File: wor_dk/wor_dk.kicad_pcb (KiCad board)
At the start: 4 copper layers, 217 x 110.1 mm, 135 parts, among them J101 Conn_01x02, J102 Conn_02x03_Odd_Even, J103 Conn_02x03_Odd_Even, J104 Conn_01x02, J201 SWD, J301 SMA, J302 Conn_02x04_Odd_Even, J303 Conn_02x06_Odd_Even, J401 USB_C_Receptacle_USB2.0_16P, J501 SWD, J502 USB_C_Receptacle_USB2.0_16P, J503 SWD, Q501 BSS84, SW201 SW_Push, SW501 SW_Push, U201 nRF52840, U202 TMUX1112PWR, U203 TMUX1112PWR, U301 Si4467, U401 FT232RL, U501 TLV1117-33, U502 LPC11U35FHI33_501, Y201 32.768kHz, Y202 32MHz, Y301 26MHz, Y501 12MHz

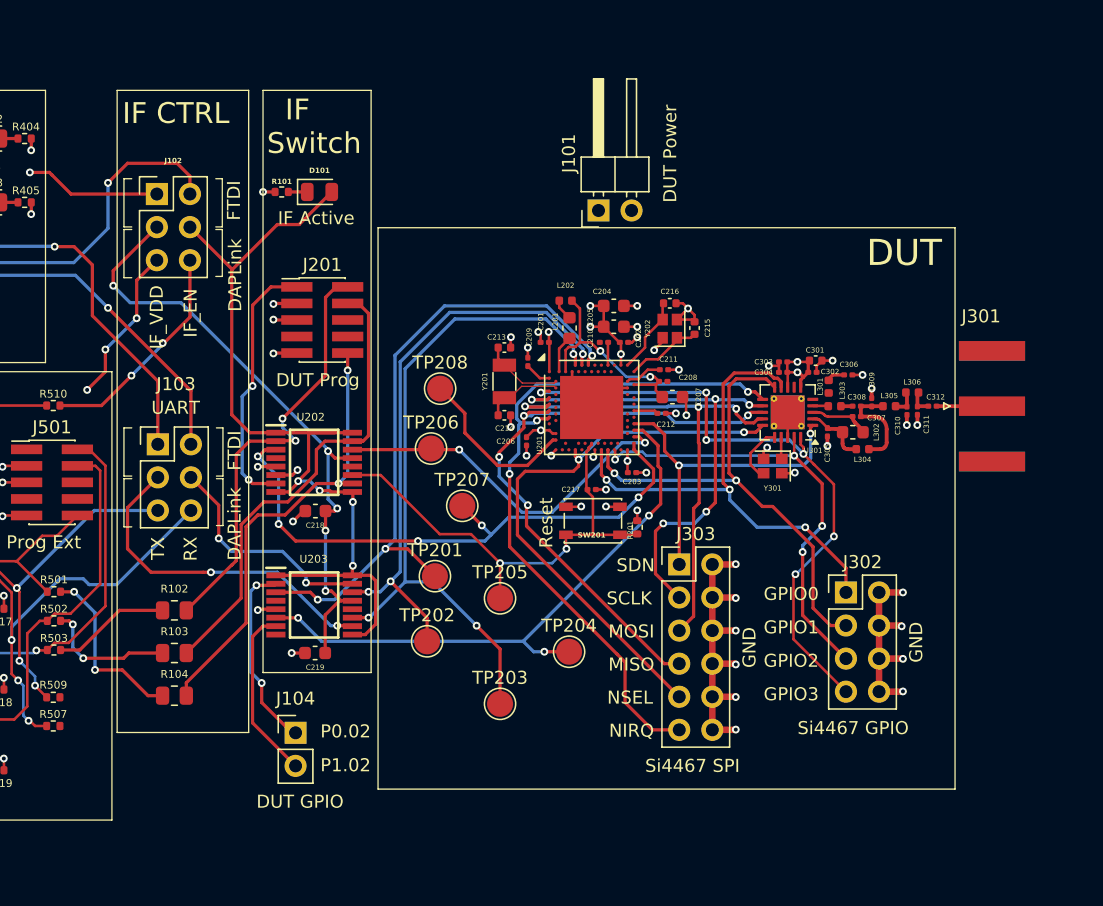
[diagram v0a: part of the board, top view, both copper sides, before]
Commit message: wor_dk: PCB: add remaining zone fills & (mostly) finalize routing
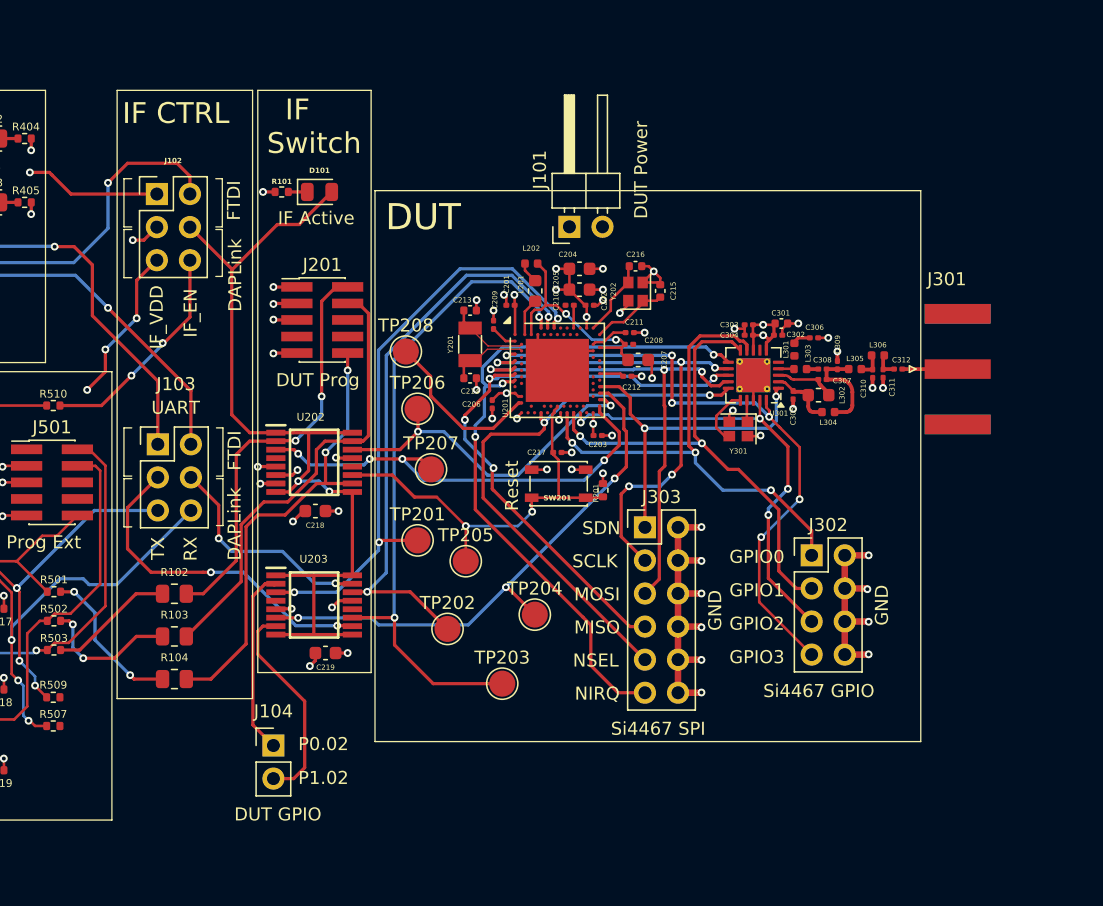
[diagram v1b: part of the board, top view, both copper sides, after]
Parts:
- moved C202 3.88 mm to (133.0, 71.6)
- moved C204 3.88 mm to (132.2, 68.8)
- moved C205 3.88 mm to (132.2, 70.4)
- moved C207 3.88 mm to (136.7, 75.8)
- moved C301 3.88 mm to (147.7, 73.0)
- moved C302 3.88 mm to (147.4, 73.9)
- moved C303 3.88 mm to (145.2, 73.1)
- moved C304 3.88 mm to (145.2, 73.9)
- moved C306 3.88 mm to (150.2, 74.1)
- moved C311 3.88 mm to (155.5, 76.8)
- moved L301 3.88 mm to (148.7, 75.0)
- moved C213 3.88 mm to (123.8, 72.0)
- moved C214 3.88 mm to (123.8, 77.2)
- moved Y201 3.88 mm to (123.8, 74.6)
- moved C201 3.88 mm to (126.9, 71.6)
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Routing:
- net /VDD_AUX: track 48.6 -> 7.24 mm
- net /Main MCU/SWDIO_: track 45.6 -> 35.0 mm, vias 5 -> 4
- net /Main MCU/NRESET_: track 36.4 -> 32.6 mm
- net /Main MCU/P1.02_: track 45.4 -> 42.2 mm
- net /P1.02: track 13.4 -> 16.3 mm
- net /Main MCU/P0.02_: track 49.8 -> 47.5 mm
- net /NRESET: track 13.8 -> 11.8 mm
- net VDD_DUT: track 46.6 -> 45.1 mm
- net /Main MCU/P0.31_: track 52.1 -> 50.6 mm, vias 3 -> 2
- net /Main MCU/SWDIO: track 33.4 -> 32.0 mm
- net /Main MCU/SWCLK: track 36.6 -> 35.3 mm
- net /IF_EN: track 68.1 -> 69.2 mm, vias 4 -> 2
- net /Main MCU/VDD_DUT_OUT: track 20.1 -> 19.1 mm
- net /Main MCU/SWCLK_: track 27.7 -> 26.8 mm
- net /Main MCU/NRESET: track 35.8 -> 35.0 mm
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- added copper zone on In2.Cu, net /VDD_AUX
- added copper zone on In2.Cu, net VDD_DUT

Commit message: wor_dk: PCB: fix some DRC issues
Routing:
- net GND: track 148.3 -> 216.7 mm, vias 79 -> 111
- net /Transceiver/NIRQ: track 54.5 -> 52.0 mm
- net VDD_PROG: track 31.8 -> 30.7 mm
- net /Transceiver/MOSI: track 39.0 -> 39.6 mm
- net /Transceiver/GPIO0: track 39.8 -> 39.3 mm
- net /Main MCU/P0.02_: track 47.5 -> 47.0 mm
- net VDD_DUT: track 45.1 -> 44.9 mm, vias 11 -> 12

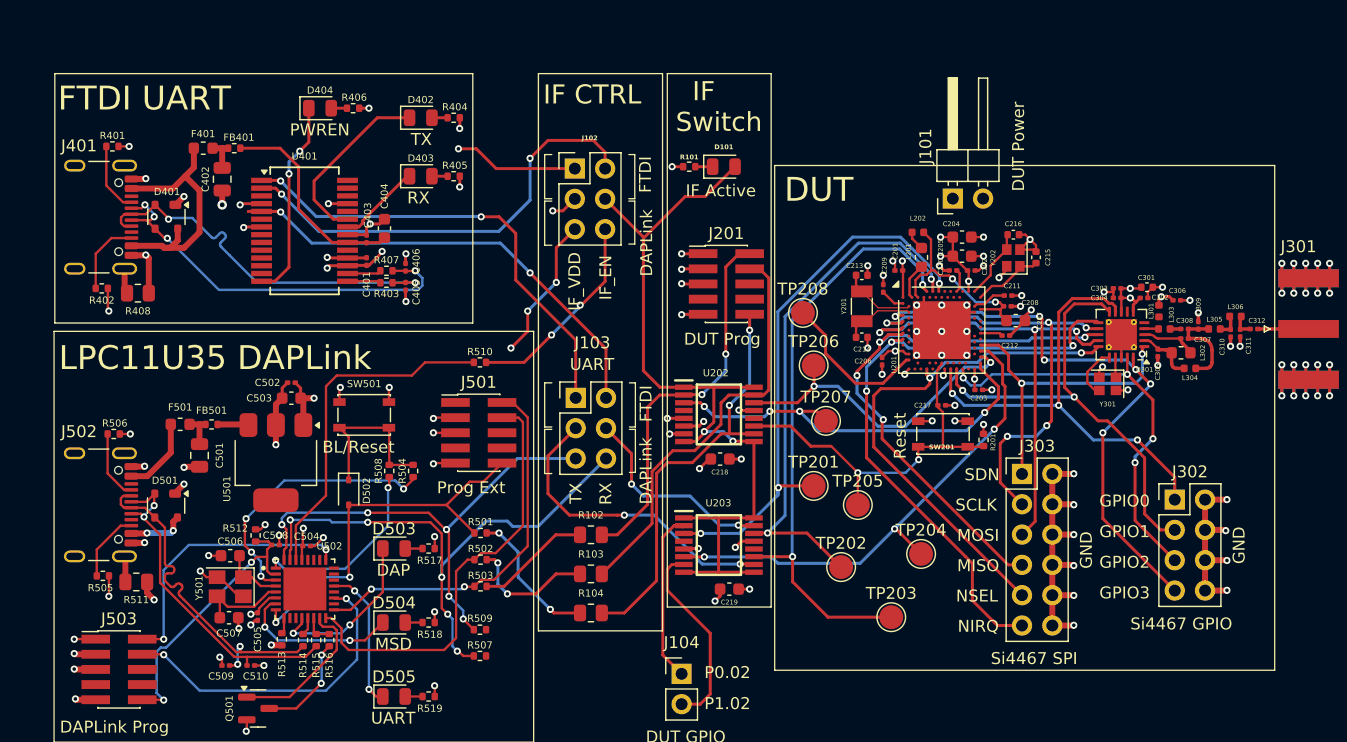
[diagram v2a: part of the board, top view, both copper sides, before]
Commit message: wor_dk: PCB: fix most DRC errors
The remaining errors are all related to the LPC11U35 footprint.
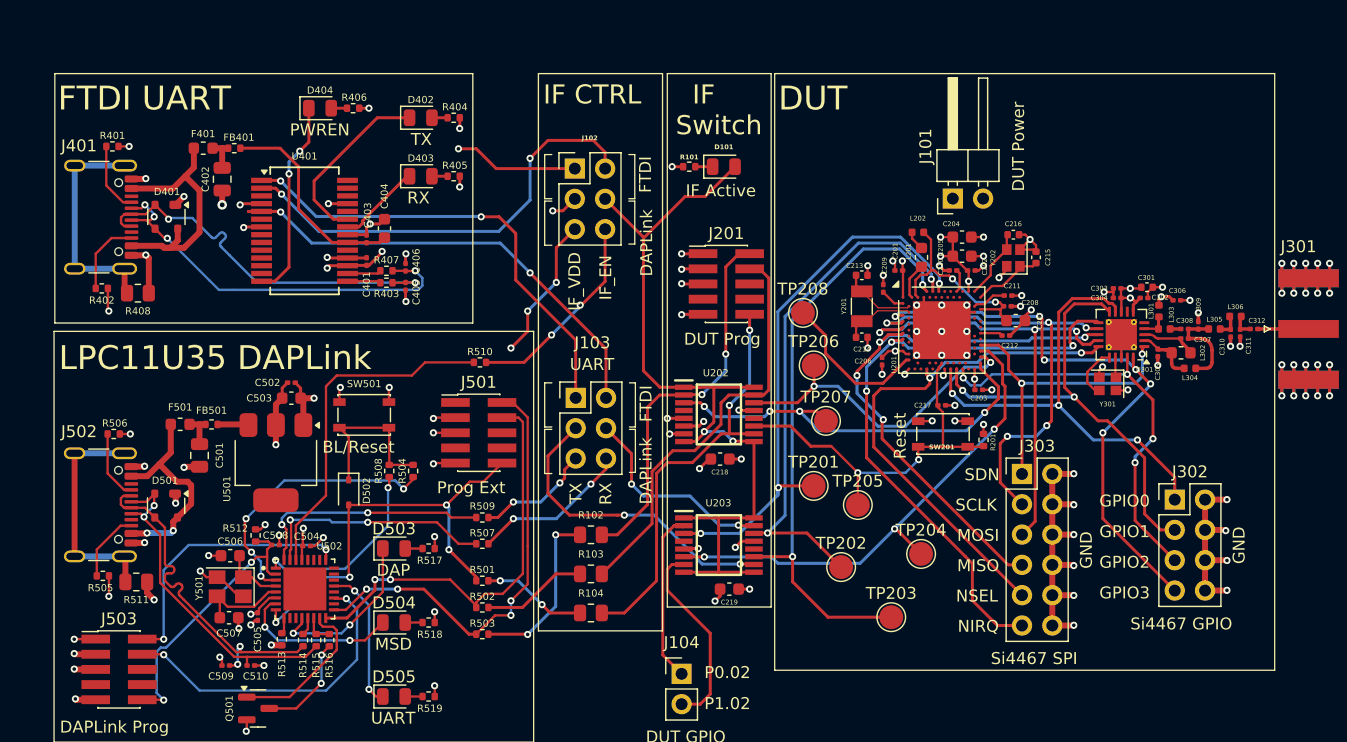
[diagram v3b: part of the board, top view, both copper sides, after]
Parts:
- moved R507 9.40 mm to (92.0, 94.5)
- moved R509 9.40 mm to (92.0, 92.3)
- moved R502 4.01 mm to (92.0, 99.8)
- moved R503 4.01 mm to (92.0, 102.1)
- moved R501 4.01 mm to (92.0, 97.6)
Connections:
- R507 pad 1: /RXD_DAP -> /LPC11U35 DAPLink Programmer/RXD
- R509 pad 1: /TXD_DAP -> /LPC11U35 DAPLink Programmer/TXD
- R510 pad 1: /DTR_DAP -> /LPC11U35 DAPLink Programmer/DTR
- U502 pad 30: /DTR_DAP -> /LPC11U35 DAPLink Programmer/DTR
- U502 pad 31: /RXD_DAP -> /LPC11U35 DAPLink Programmer/RXD
- U502 pad 32: /TXD_DAP -> /LPC11U35 DAPLink Programmer/TXD
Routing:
- net /RXD_DAP: track 47.4 -> 13.3 mm, vias 5 -> 2
- net /TXD_DAP: track 40.9 -> 9.79 mm, vias 5 -> 2
- net /DTR_DAP: track 46.0 -> 17.2 mm
- net /LPC11U35 DAPLink Programmer/DTR: track 0.00 -> 28.8 mm
- net /LPC11U35 DAPLink Programmer/TXD: track 0.00 -> 20.4 mm, vias 0 -> 2
- net /LPC11U35 DAPLink Programmer/RXD: track 0.00 -> 19.8 mm, vias 0 -> 2
- net Net-(J502-SHIELD): track 2.18 -> 19.2 mm
- net Net-(J401-SHIELD): track 2.13 -> 19.1 mm
- net Net-(D501-VCC): track 11.4 -> 17.9 mm
- net /LPC11U35 DAPLink Programmer/TGT_SWDIO: track 31.9 -> 37.6 mm, vias 2 -> 4
- net /SWDIO: track 9.62 -> 14.7 mm, vias 0 -> 2
- net /LPC11U35 DAPLink Programmer/TGT_NRESET: track 32.5 -> 36.6 mm, vias 2 -> 4
- net /NRESET: track 11.8 -> 8.80 mm
- net /SWCLK: track 10.8 -> 8.84 mm, vias 2 -> 0
- net /LPC11U35 DAPLink Programmer/TGT_SWCLK: track 36.5 -> 35.5 mm, vias 0 -> 2
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
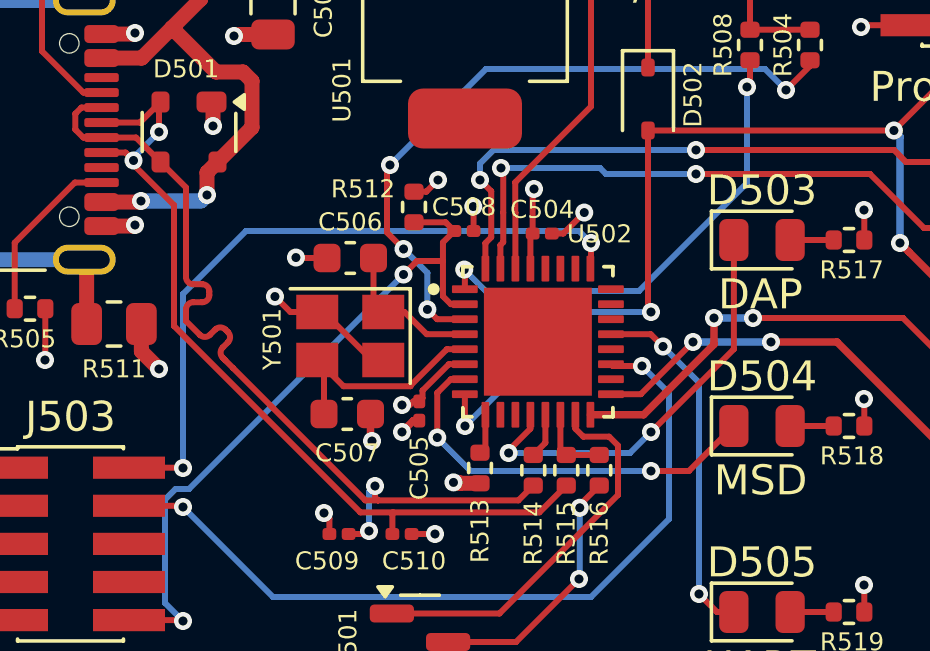
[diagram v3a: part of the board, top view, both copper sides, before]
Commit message: wor_dk: PCB: use KiCAD HVQFN-32 footprint instead of downloaded
This fixes all remaining DRC issues.
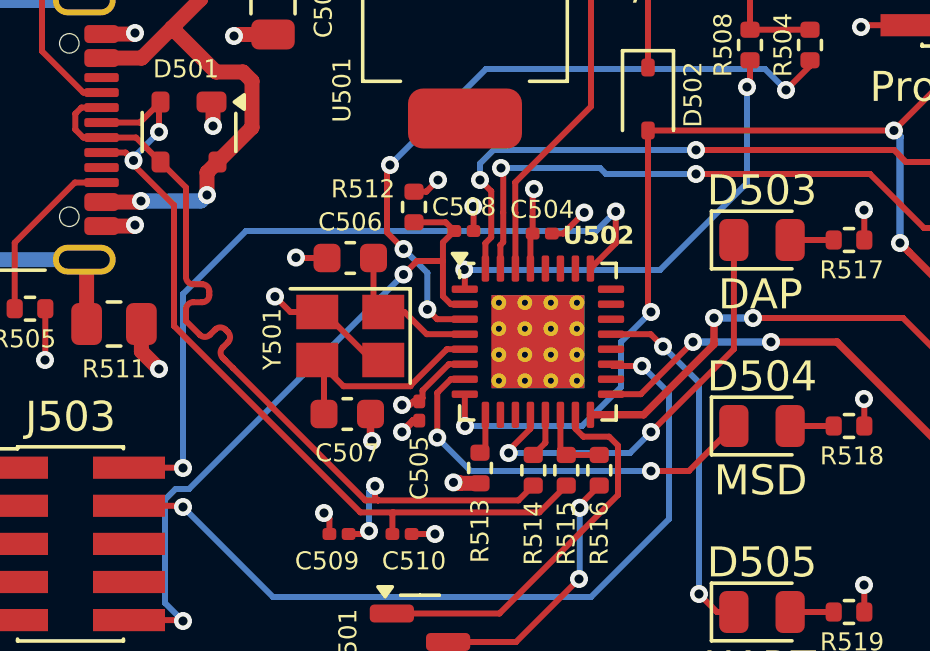
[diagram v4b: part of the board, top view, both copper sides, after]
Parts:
- U502: footprint NXP:QFN50P500X500X85-33N -> Package_DFN_QFN:HVQFN-32-1EP_5x5mm_P0.5mm_EP3.1x3.1mm_ThermalVias
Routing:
- net /LPC11U35 DAPLink Programmer/IF_SWDIO: track 23.1 -> 25.4 mm
- net /LPC11U35 DAPLink Programmer/TGT_NRESET: track 36.6 -> 37.5 mm
- net /LPC11U35 DAPLink Programmer/TGT_NRESET_FB_ISP: track 16.0 -> 15.4 mm

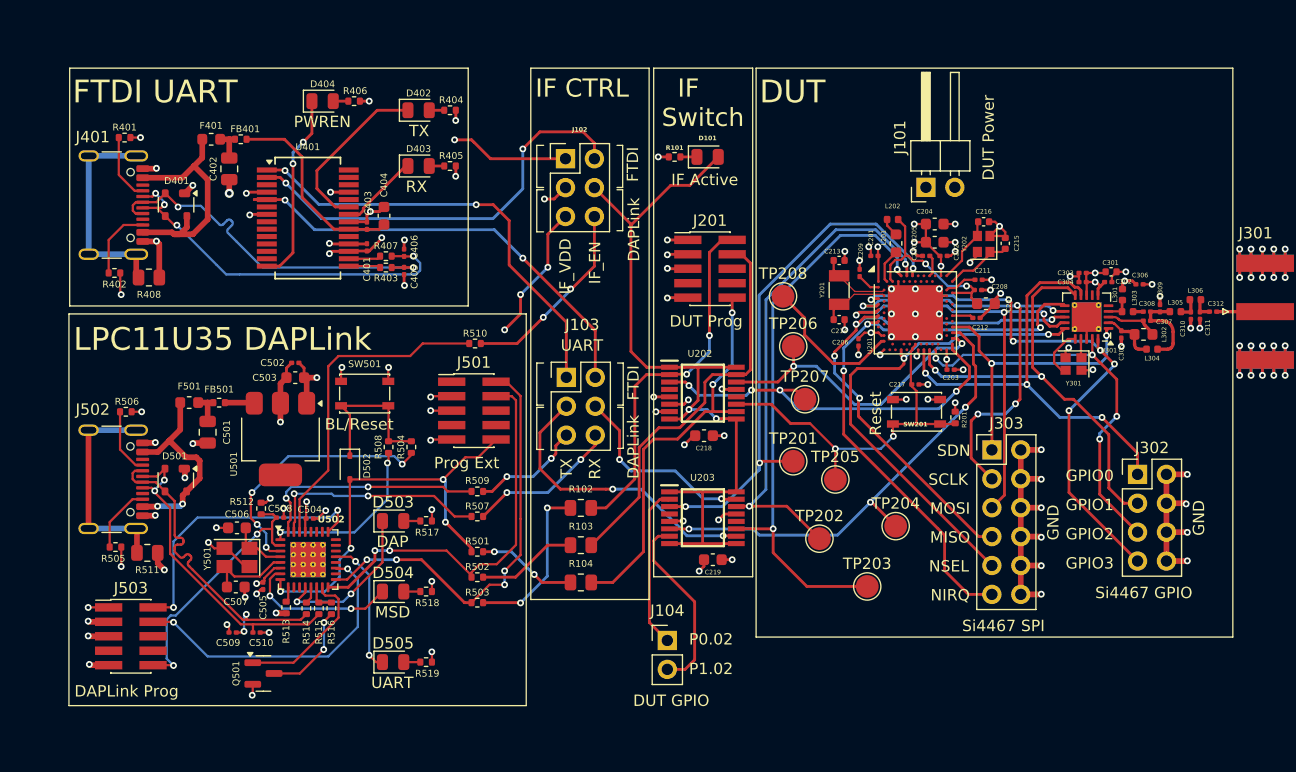
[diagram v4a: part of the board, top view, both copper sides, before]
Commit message: wor_dk: add M2.5 screw holes
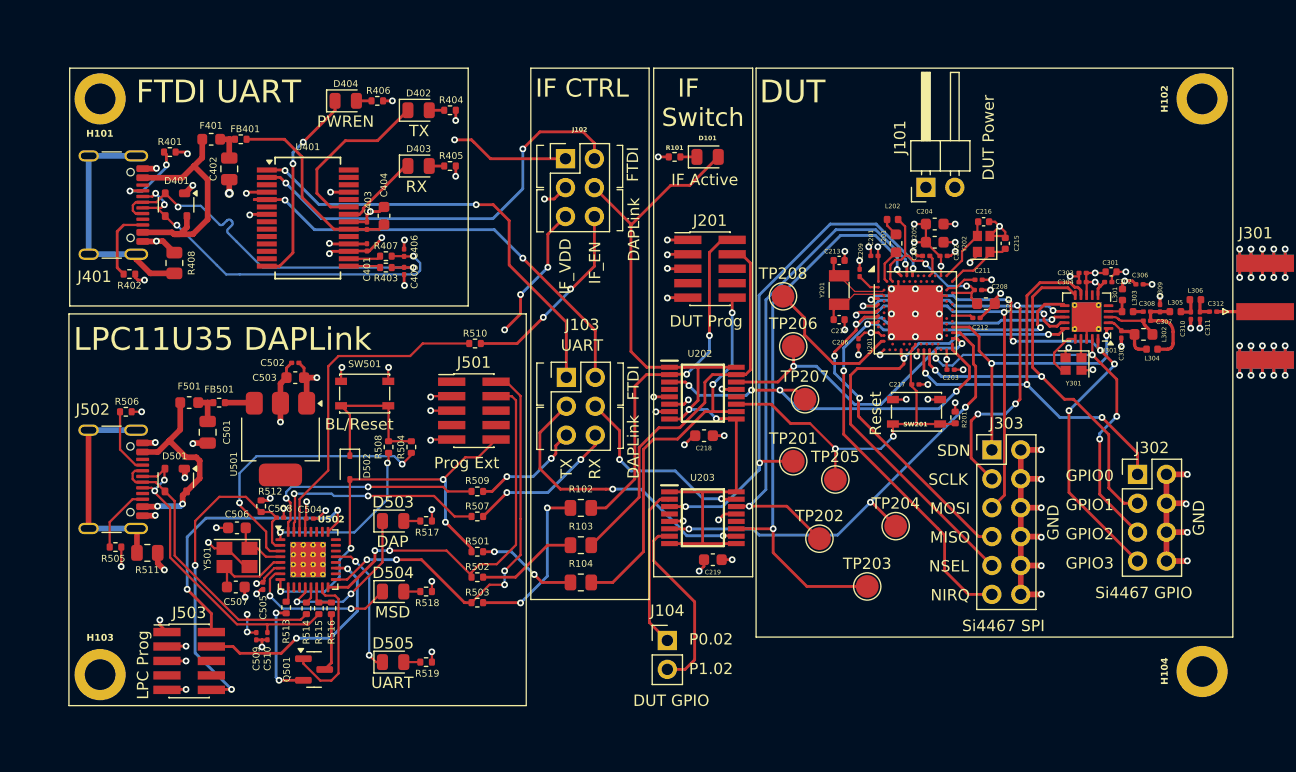
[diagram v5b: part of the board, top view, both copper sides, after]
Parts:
- added H101: MountingHole_Pad, MountingHole:MountingHole_2.7mm_M2.5_ISO7380_Pad, F.Cu at (58.9, 57.8)
- added H102: MountingHole_Pad, MountingHole:MountingHole_2.7mm_M2.5_ISO7380_Pad, F.Cu at (155.7, 57.8)
- added H103: MountingHole_Pad, MountingHole:MountingHole_2.7mm_M2.5_ISO7380_Pad, F.Cu at (58.9, 108.4)
- added H104: MountingHole_Pad, MountingHole:MountingHole_2.7mm_M2.5_ISO7380_Pad, F.Cu at (155.7, 108.1)
- moved J503 5.57 mm to (66.7, 107.2)
- moved Q501 4.46 mm to (77.7, 108.0)
- moved R401 4.17 mm to (65.0, 62.5)
- moved R408 2.58 mm to (65.4, 72.2), turned to 90 degrees
- moved C509 2.10 mm to (72.6, 105.0), turned to 90 degrees
- moved D404 2.04 mm to (80.4, 58.0)
- moved R406 2.04 mm to (83.2, 58.0)
- moved R402 1.32 mm to (61.4, 73.2)
- moved C510 1.00 mm to (73.5, 105.0), turned to 90 degrees
- moved R512 0.20 mm to (73.0, 93.6)
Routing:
- net /LPC11U35 DAPLink Programmer/IF_SWCLK: track 26.9 -> 19.7 mm
- net VDD_PROG: track 30.7 -> 37.4 mm
- net /LPC11U35 DAPLink Programmer/IF_NRESET: track 23.3 -> 29.9 mm
- net Net-(Q501-D): track 8.63 -> 5.11 mm, vias 2 -> 0
- net /LPC11U35 DAPLink Programmer/TGT_NRESET_FB: track 22.9 -> 25.4 mm, vias 4 -> 2
- net Net-(J401-SHIELD): track 19.1 -> 21.3 mm
- net GND: track 216.4 -> 214.3 mm, vias 111 -> 110
- net /LPC11U35 DAPLink Programmer/USB_D-: track 29.6 -> 27.8 mm
- net Net-(D404-K): track 16.8 -> 17.7 mm
- net Net-(J401-CC1): track 5.97 -> 6.62 mm, vias 0 -> 2
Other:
- board text added: "LPC Prog"
- board text removed: "DAPLink Prog"
